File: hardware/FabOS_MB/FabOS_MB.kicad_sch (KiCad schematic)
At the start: 4 parts

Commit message: led
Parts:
- renumbered H1 to H101, H2 to H102, H3 to H103, H4 to H104
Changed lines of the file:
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@@
 		(dnp no)
 		(fields_autoplaced yes)
-		(property "Reference" "#PWR0101"
+		(property "Reference" "#PWR0102"
 			(at 67.31 34.29 0)
 			(effects
@@
 			(project "FabOS_MB"
 				(path "/09377d5d-727f-4ff4-92c8-7a0483d23f1e"
-					(reference "#PWR0101")
+					(reference "#PWR0102")
 					(unit 1)
 				)
@@
 		(dnp no)
 		(fields_autoplaced yes)
-		(property "Reference" "H1"
+		(property "Reference" "H101"
 			(at 57.15 54.6099 90)
 			(effects
@@
 			(project "FabOS_MB"
 				(path "/09377d5d-727f-4ff4-92c8-7a0483d23f1e"
-					(reference "H1")
+					(reference "H101")
 					(unit 1)
 				)
@@
 		(dnp no)
 		(fields_autoplaced yes)
-		(property "Reference" "H3"
+		(property "Reference" "H103"
 			(at 57.15 80.0099 90)
 			(effects
@@
 			(project "FabOS_MB"
 				(path "/09377d5d-727f-4ff4-92c8-7a0483d23f1e"
-					(reference "H3")
+					(reference "H103")
 					(unit 1)
 				)
@@
 		(dnp no)
 		(fields_autoplaced yes)
-		(property "Reference" "#PWR01"
+		(property "Reference" "#PWR0101"
 			(at 41.91 106.68 0)
 			(effects
@@
 			(project "FabOS_MB"
 				(path "/09377d5d-727f-4ff4-92c8-7a0483d23f1e"
-					(reference "#PWR01")
+					(reference "#PWR0101")
 					(unit 1)
 				)
@@
 		(dnp no)
 		(fields_autoplaced yes)
-		(property "Reference" "#FLG01"
+		(property "Reference" "#FLG0101"
 			(at 69.215 31.75 0)
 			(effects
@@
 			(project ""
 				(path "/09377d5d-727f-4ff4-92c8-7a0483d23f1e"
-					(reference "#FLG01")
+					(reference "#FLG0101")
 					(unit 1)
 				)
@@
 		(dnp no)
 		(fields_autoplaced yes)
-		(property "Reference" "H2"
+		(property "Reference" "H102"
 			(at 57.15 67.3099 90)
 			(effects
@@
 			(project "FabOS_MB"
 				(path "/09377d5d-727f-4ff4-92c8-7a0483d23f1e"
-					(reference "H2")
+					(reference "H102")
 					(unit 1)
 				)
@@
 		(dnp no)
 		(fields_autoplaced yes)
-		(property "Reference" "H4"
+		(property "Reference" "H104"
 			(at 57.15 92.7099 90)
 			(effects
@@
 			(project "FabOS_MB"
 				(path "/09377d5d-727f-4ff4-92c8-7a0483d23f1e"
-					(reference "H4")
-					(unit 1)
-				)
+					(reference "H104")
+					(unit 1)
+				)

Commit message: create pcb
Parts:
- H101, H102, H103, H104: footprint MountingHole:MountingHole_3.2mm_M3_DIN965_Pad -> MountingHole:MountingHole_3.2mm_M3_Pad_Via
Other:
- moved on the sheet: H101, H102, H103, H104
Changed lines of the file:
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@@
 	)
 	(junction
-		(at 41.91 93.98)
+		(at 39.37 67.31)
 		(diameter 0)
 		(color 0 0 0 0)
 	)
 	(junction
-		(at 41.91 68.58)
+		(at 39.37 57.15)
 		(diameter 0)
 		(color 0 0 0 0)
 	)
 	(junction
-		(at 41.91 81.28)
+		(at 39.37 62.23)
 		(diameter 0)
 		(color 0 0 0 0)
@@
 	(wire
 		(pts
-			(xy 50.8 55.88) (xy 41.91 55.88)
+			(xy 48.26 52.07) (xy 39.37 52.07)
 		)
 		(stroke
@@
 	(wire
 		(pts
-			(xy 41.91 93.98) (xy 50.8 93.98)
-		)
-		(stroke
-			(width 0)
-			(type default)
-		)
-	)
-	(wire
-		(pts
-			(xy 41.91 68.58) (xy 41.91 81.28)
-		)
-		(stroke
-			(width 0)
-			(type default)
-		)
-	)
-	(wire
-		(pts
-			(xy 41.91 68.58) (xy 50.8 68.58)
+			(xy 39.37 67.31) (xy 48.26 67.31)
+		)
+		(stroke
+			(width 0)
+			(type default)
+		)
+	)
+	(wire
+		(pts
+			(xy 39.37 57.15) (xy 39.37 62.23)
+		)
+		(stroke
+			(width 0)
+			(type default)
+		)
+	)
+	(wire
+		(pts
+			(xy 39.37 57.15) (xy 48.26 57.15)
 		)
 		(stroke
@@
 	(wire
 		(pts
-			(xy 41.91 93.98) (xy 41.91 100.33)
+			(xy 39.37 67.31) (xy 39.37 73.66)
 		)
 		(stroke
@@
 	(wire
 		(pts
-			(xy 41.91 81.28) (xy 50.8 81.28)
-		)
-		(stroke
-			(width 0)
-			(type default)
-		)
-	)
-	(wire
-		(pts
-			(xy 41.91 55.88) (xy 41.91 68.58)
+			(xy 39.37 62.23) (xy 48.26 62.23)
+		)
+		(stroke
+			(width 0)
+			(type default)
+		)
+	)
+	(wire
+		(pts
+			(xy 39.37 52.07) (xy 39.37 57.15)
 		)
 		(stroke
@@
 	(wire
 		(pts
-			(xy 41.91 81.28) (xy 41.91 93.98)
+			(xy 39.37 62.23) (xy 39.37 67.31)
 		)
 		(stroke
@@
 	(symbol
 		(lib_id "Mechanical:MountingHole_Pad")
-		(at 53.34 55.88 270)
+		(at 50.8 52.07 270)
 		(unit 1)
 		(exclude_from_sim yes)
@@
 		(fields_autoplaced yes)
 		(property "Reference" "H101"
-			(at 57.15 54.6099 90)
+			(at 54.61 50.7999 90)
 			(effects
 				(font
@@
 		)
 		(property "Value" "MountingHole_Pad"
-			(at 57.15 57.1499 90)
+			(at 54.61 53.3399 90)
 			(effects
 				(font
@@
 			)
 		)
-		(property "Footprint" "MountingHole:MountingHole_3.2mm_M3_DIN965_Pad"
-			(at 53.34 55.88 0)
+		(property "Footprint" "MountingHole:MountingHole_3.2mm_M3_Pad_Via"
+			(at 50.8 52.07 0)
 			(effects
 				(font
@@
 		)
 		(property "Datasheet" "~"
-			(at 53.34 55.88 0)
+			(at 50.8 52.07 0)
 			(effects
 				(font
@@
 		)
 		(property "Description" "Mounting Hole with connection"
-			(at 53.34 55.88 0)
+			(at 50.8 52.07 0)
 			(effects
 				(font
@@
 	(symbol
 		(lib_id "Mechanical:MountingHole_Pad")
-		(at 53.34 81.28 270)
+		(at 50.8 62.23 270)
 		(unit 1)
 		(exclude_from_sim yes)
@@
 		(fields_autoplaced yes)
 		(property "Reference" "H103"
-			(at 57.15 80.0099 90)
+			(at 54.61 60.9599 90)
 			(effects
 				(font
@@
 		)
 		(property "Value" "MountingHole_Pad"
-			(at 57.15 82.5499 90)
+			(at 54.61 63.4999 90)
 			(effects
 				(font
@@
 			)
 		)
-		(property "Footprint" "MountingHole:MountingHole_3.2mm_M3_DIN965_Pad"
-			(at 53.34 81.28 0)
+		(property "Footprint" "MountingHole:MountingHole_3.2mm_M3_Pad_Via"
+			(at 50.8 62.23 0)
 			(effects
 				(font
@@
 		)
 		(property "Datasheet" "~"
-			(at 53.34 81.28 0)
+			(at 50.8 62.23 0)
 			(effects
 				(font
@@
 		)
 		(property "Description" "Mounting Hole with connection"
-			(at 53.34 81.28 0)
+			(at 50.8 62.23 0)
 			(effects
 				(font
@@
 	(symbol
 		(lib_id "power:GND")
-		(at 41.91 100.33 0)
+		(at 39.37 73.66 0)
 		(unit 1)
 		(exclude_from_sim no)
@@
 		(fields_autoplaced yes)
 		(property "Reference" "#PWR0101"
-			(at 41.91 106.68 0)
+			(at 39.37 80.01 0)
 			(effects
 				(font
@@
 		)
 		(property "Value" "GND"
-			(at 41.91 105.41 0)
+			(at 39.37 78.74 0)
 			(effects
 				(font
@@
 		)
 		(property "Footprint" ""
-			(at 41.91 100.33 0)
+			(at 39.37 73.66 0)
 			(effects
 				(font
@@
 		)
 		(property "Datasheet" ""
-			(at 41.91 100.33 0)
+			(at 39.37 73.66 0)
 			(effects
 				(font
@@
 		)
 		(property "Description" "Power symbol creates a global label with name \"GND\" , ground"
-			(at 41.91 100.33 0)
+			(at 39.37 73.66 0)
 			(effects
 				(font
@@
 	(symbol
 		(lib_id "Mechanical:MountingHole_Pad")
-		(at 53.34 68.58 270)
+		(at 50.8 57.15 270)
 		(unit 1)
 		(exclude_from_sim yes)
@@
 		(fields_autoplaced yes)
 		(property "Reference" "H102"
-			(at 57.15 67.3099 90)
+			(at 54.61 55.8799 90)
 			(effects
 				(font
@@
 		)
 		(property "Value" "MountingHole_Pad"
-			(at 57.15 69.8499 90)
+			(at 54.61 58.4199 90)
 			(effects
 				(font
@@
 			)
 		)
-		(property "Footprint" "MountingHole:MountingHole_3.2mm_M3_DIN965_Pad"
-			(at 53.34 68.58 0)
+		(property "Footprint" "MountingHole:MountingHole_3.2mm_M3_Pad_Via"
+			(at 50.8 57.15 0)
 			(effects
 				(font
@@
 		)
 		(property "Datasheet" "~"
-			(at 53.34 68.58 0)
+			(at 50.8 57.15 0)
 			(effects
 				(font
@@
 		)
 		(property "Description" "Mounting Hole with connection"
-			(at 53.34 68.58 0)
+			(at 50.8 57.15 0)
 			(effects
 				(font
@@
 	(symbol
 		(lib_id "Mechanical:MountingHole_Pad")
-		(at 53.34 93.98 270)
+		(at 50.8 67.31 270)
 		(unit 1)
 		(exclude_from_sim yes)
@@
 		(fields_autoplaced yes)
 		(property "Reference" "H104"
-			(at 57.15 92.7099 90)
+			(at 54.61 66.0399 90)
 			(effects
 				(font
@@
 		)
 		(property "Value" "MountingHole_Pad"
-			(at 57.15 95.2499 90)
+			(at 54.61 68.5799 90)
 			(effects
 				(font
@@
 			)
 		)
-		(property "Footprint" "MountingHole:MountingHole_3.2mm_M3_DIN965_Pad"
-			(at 53.34 93.98 0)
+		(property "Footprint" "MountingHole:MountingHole_3.2mm_M3_Pad_Via"
+			(at 50.8 67.31 0)
 			(effects
 				(font
@@
 		)
 		(property "Datasheet" "~"
-			(at 53.34 93.98 0)
+			(at 50.8 67.31 0)
 			(effects
 				(font
@@
 		)
 		(property "Description" "Mounting Hole with connection"
-			(at 53.34 93.98 0)
-			(effects
-				(font
+			(at 50.8 67.31 0)
+			(effects
+				(font

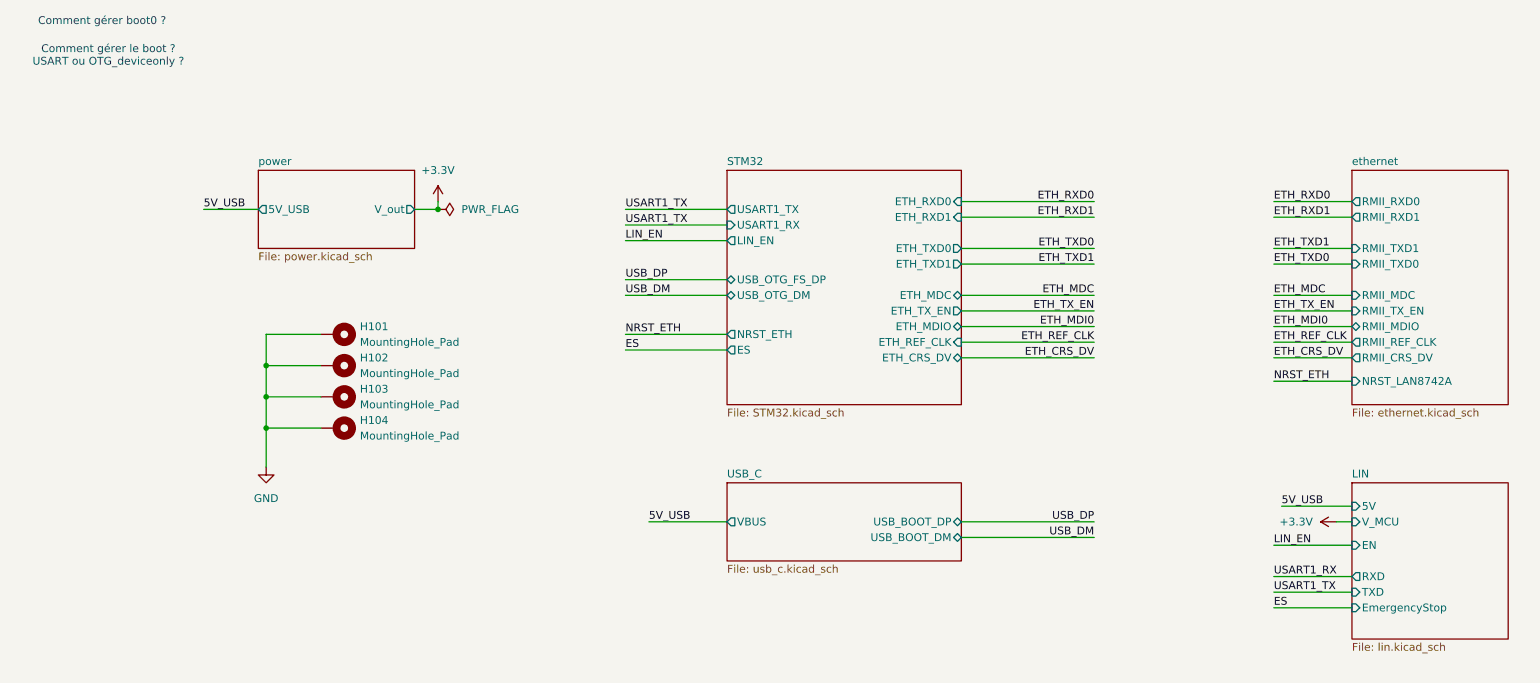
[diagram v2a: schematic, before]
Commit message: update components placement
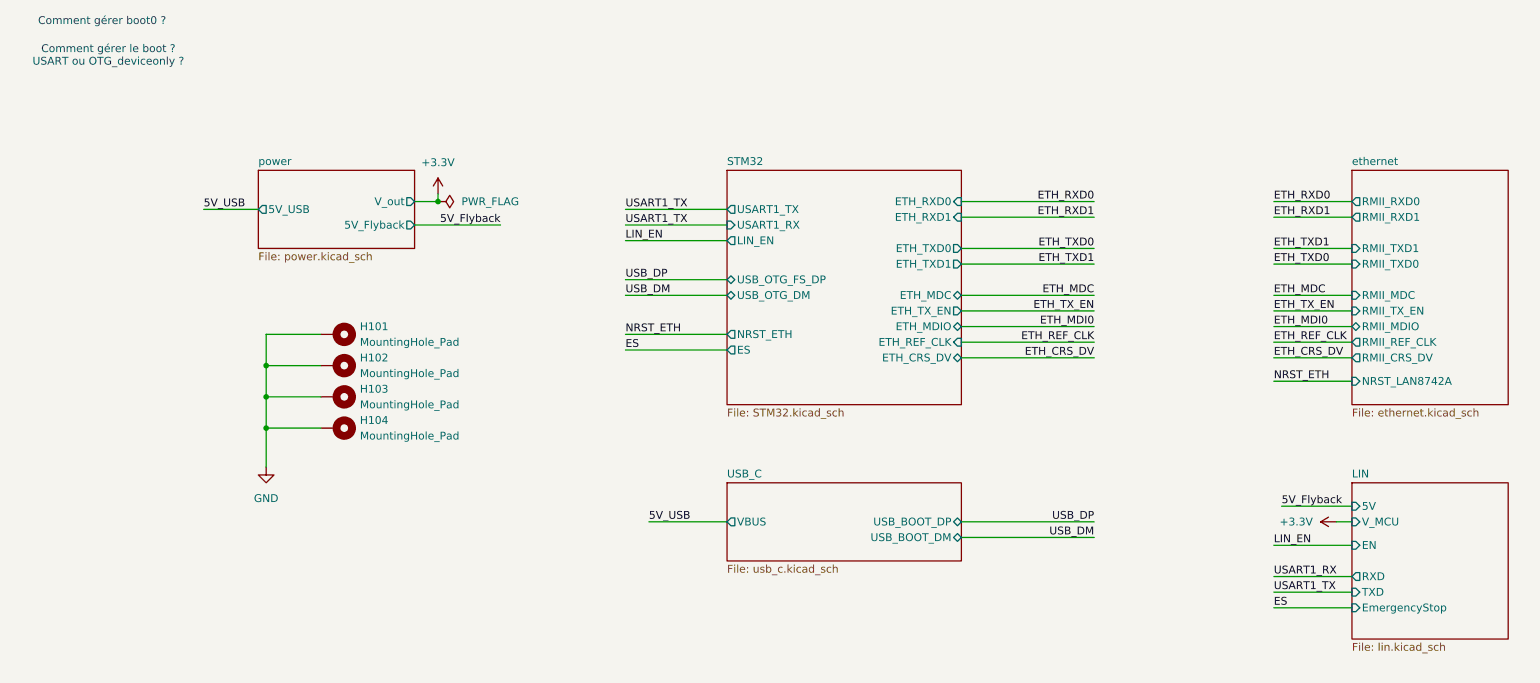
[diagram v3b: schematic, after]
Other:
- sheet power ports: added 5V_Flyback; removed none
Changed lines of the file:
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@@
 	)
 	(junction
-		(at 67.31 31.75)
+		(at 67.31 30.48)
 		(diameter 0)
 		(color 0 0 0 0)
@@
 	(wire
 		(pts
-			(xy 67.31 31.75) (xy 63.5 31.75)
+			(xy 67.31 30.48) (xy 63.5 30.48)
 		)
 		(stroke
@@
 	(wire
 		(pts
+			(xy 63.5 34.29) (xy 77.47 34.29)
+		)
+		(stroke
+			(width 0)
+			(type default)
+		)
+	)
+	(wire
+		(pts
 			(xy 152.4 48.26) (xy 173.99 48.26)
 		)
@@
 	(wire
 		(pts
-			(xy 67.31 30.48) (xy 67.31 31.75)
+			(xy 67.31 29.21) (xy 67.31 30.48)
 		)
 		(stroke
@@
 		)
 	)
-	(label "5V_USB"
-		(at 204.47 80.01 0)
-		(fields_autoplaced yes)
-		(effects
-			(font
-				(size 1.27 1.27)
-			)
-			(justify left bottom)
-		)
-	)
 	(label "ES"
 		(at 97.79 54.61 0)
@@
 		)
 	)
+	(label "5V_Flyback"
+		(at 77.47 34.29 180)
+		(fields_autoplaced yes)
+		(effects
+			(font
+				(size 1.27 1.27)
+			)
+			(justify right bottom)
+		)
+	)
 	(label "USART1_RX"
 		(at 203.2 91.44 0)
@@
 		)
 	)
+	(label "5V_Flyback"
+		(at 204.47 80.01 0)
+		(fields_autoplaced yes)
+		(effects
+			(font
+				(size 1.27 1.27)
+			)
+			(justify left bottom)
+		)
+	)
 	(label "ETH_MDI0"
 		(at 173.99 50.8 180)
@@
 	(symbol
 		(lib_id "power:+3.3V")
-		(at 67.31 30.48 0)
+		(at 67.31 29.21 0)
 		(unit 1)
 		(exclude_from_sim no)
@@
 		(fields_autoplaced yes)
 		(property "Reference" "#PWR0102"
-			(at 67.31 34.29 0)
+			(at 67.31 33.02 0)
 			(effects
 				(font
@@
 		)
 		(property "Value" "+3.3V"
-			(at 67.31 25.4 0)
+			(at 67.31 24.13 0)
 			(effects
 				(font
@@
 		)
 		(property "Footprint" ""
-			(at 67.31 30.48 0)
+			(at 67.31 29.21 0)
 			(effects
 				(font
@@
 		)
 		(property "Datasheet" ""
-			(at 67.31 30.48 0)
+			(at 67.31 29.21 0)
 			(effects
 				(font
@@
 		)
 		(property "Description" "Power symbol creates a global label with name \"+3.3V\""
-			(at 67.31 30.48 0)
+			(at 67.31 29.21 0)
 			(effects
 				(font
@@
 	(symbol
 		(lib_id "power:PWR_FLAG")
-		(at 67.31 31.75 270)
+		(at 67.31 30.48 270)
 		(unit 1)
 		(exclude_from_sim no)
@@
 		(fields_autoplaced yes)
 		(property "Reference" "#FLG0101"
-			(at 69.215 31.75 0)
+			(at 69.215 30.48 0)
 			(effects
 				(font
@@
 		)
 		(property "Value" "PWR_FLAG"
-			(at 71.12 31.7499 90)
+			(at 71.12 30.4799 90)
 			(effects
 				(font
@@
 		)
 		(property "Footprint" ""
-			(at 67.31 31.75 0)
+			(at 67.31 30.48 0)
 			(effects
 				(font
@@
 		)
 		(property "Datasheet" "~"
-			(at 67.31 31.75 0)
+			(at 67.31 30.48 0)
 			(effects
 				(font
@@
 		)
 		(property "Description" "Special symbol for telling ERC where power comes from"
-			(at 67.31 31.75 0)
+			(at 67.31 30.48 0)
 			(effects
 				(font
@@
 		)
 		(pin "V_out" output
-			(at 63.5 31.75 0)
-			(effects
-				(font
+			(at 63.5 30.48 0)
+			(effects
+				(font
+					(size 1.27 1.27)
+				)
+				(justify right)
+			)
+		)
+		(pin "5V_Flyback" output
+			(at 63.5 34.29 0)
+			(effects
+				(font

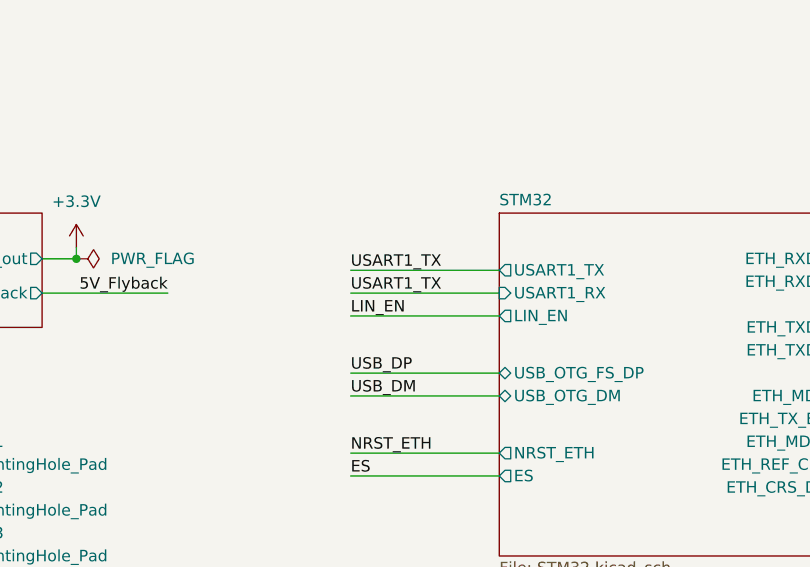
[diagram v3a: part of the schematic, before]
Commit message: update pcb
Tout les pins sont connectés. Il reste 32 violations à résoudre
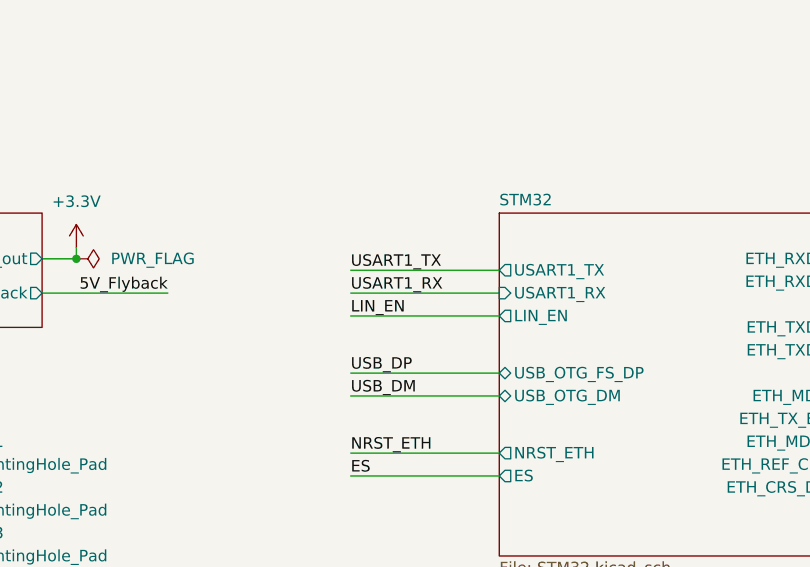
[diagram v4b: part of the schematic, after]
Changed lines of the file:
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@@
 		)
 	)
-	(label "USART1_TX"
+	(label "USART1_RX"
 		(at 97.79 34.29 0)
 		(fields_autoplaced yes)

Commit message: Modification PCB
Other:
- sheet STM32 ports: added USB_OTG_D+, USB_OTG_D-; removed USB_OTG_DM, USB_OTG_FS_DP
- sheet USB_C ports: added USB_BOOT_D+, USB_BOOT_D-; removed USB_BOOT_DM, USB_BOOT_DP
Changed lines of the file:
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@@
-		)
-	)
-	(label "USB_DM"
-		(at 173.99 85.09 180)
-		(fields_autoplaced yes)
-		(effects
-			(font
-				(size 1.27 1.27)
-			)
-			(justify right bottom)
 		)
 	)
@@
 		)
 	)
+	(label "USB_D-"
+		(at 173.99 85.09 180)
+		(fields_autoplaced yes)
+		(effects
+			(font
+				(size 1.27 1.27)
+			)
+			(justify right bottom)
+		)
+	)
 	(label "NRST_ETH"
 		(at 97.79 52.07 0)
@@
 		)
 	)
-	(label "USB_DM"
+	(label "USB_D-"
 		(at 97.79 45.72 0)
 		(fields_autoplaced yes)
@@
 		)
 	)
-	(label "USB_DP"
+	(label "USB_D+"
 		(at 173.99 82.55 180)
 		(fields_autoplaced yes)
@@
 		)
 	)
-	(label "USB_DP"
+	(label "USB_D+"
 		(at 97.79 43.18 0)
 		(fields_autoplaced yes)
@@
 			)
 		)
-		(pin "USB_BOOT_DM" bidirectional
-			(at 152.4 85.09 0)
-			(effects
-				(font
-					(size 1.27 1.27)
-				)
-				(justify right)
-			)
-		)
-		(pin "USB_BOOT_DP" bidirectional
-			(at 152.4 82.55 0)
-			(effects
-				(font
-					(size 1.27 1.27)
-				)
-				(justify right)
-			)
-		)
 		(pin "VBUS" output
 			(at 114.3 82.55 180)
@@
 				)
 				(justify left)
+			)
+		)
+		(pin "USB_BOOT_D-" bidirectional
+			(at 152.4 85.09 0)
+			(effects
+				(font
+					(size 1.27 1.27)
+				)
+				(justify right)
+			)
+		)
+		(pin "USB_BOOT_D+" bidirectional
+			(at 152.4 82.55 0)
+			(effects
+				(font
+					(size 1.27 1.27)
+				)
+				(justify right)
 			)
 		)
@@
 			)
 		)
-		(pin "USB_OTG_DM" bidirectional
-			(at 114.3 45.72 180)
-			(effects
-				(font
-					(size 1.27 1.27)
-				)
-				(justify left)
-			)
-		)
-		(pin "USB_OTG_FS_DP" bidirectional
-			(at 114.3 43.18 180)
-			(effects
-				(font
-					(size 1.27 1.27)
-				)
-				(justify left)
-			)
-		)
 		(pin "ETH_REF_CLK" input
 			(at 152.4 53.34 0)
@@
 			(effects
 				(font
+					(size 1.27 1.27)
+				)
+				(justify left)
+			)
+		)
+		(pin "USB_OTG_D+" bidirectional
+			(at 114.3 43.18 180)
+			(effects
+				(font
+					(size 1.27 1.27)
+				)
+				(justify left)
+			)
+		)
+		(pin "USB_OTG_D-" bidirectional
+			(at 114.3 45.72 180)
+			(effects
+				(font
